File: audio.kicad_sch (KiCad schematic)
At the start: 36 parts, among them J16 Conn_01x02, J20 Audio Output, Q5 2N3904, Q6 2N3904, Q7 2N3904, Q8 2N7000

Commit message: Small drawing cleanups.
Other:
- company: (none) -> EZ Electronics
- title: (none) -> Arduino Mega2560 K3NG Keyer - Audio Circuits
- moved on the sheet: C10, C11, C12, C13, C14, C15, C16, C17, C8, C9, J20, JP4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

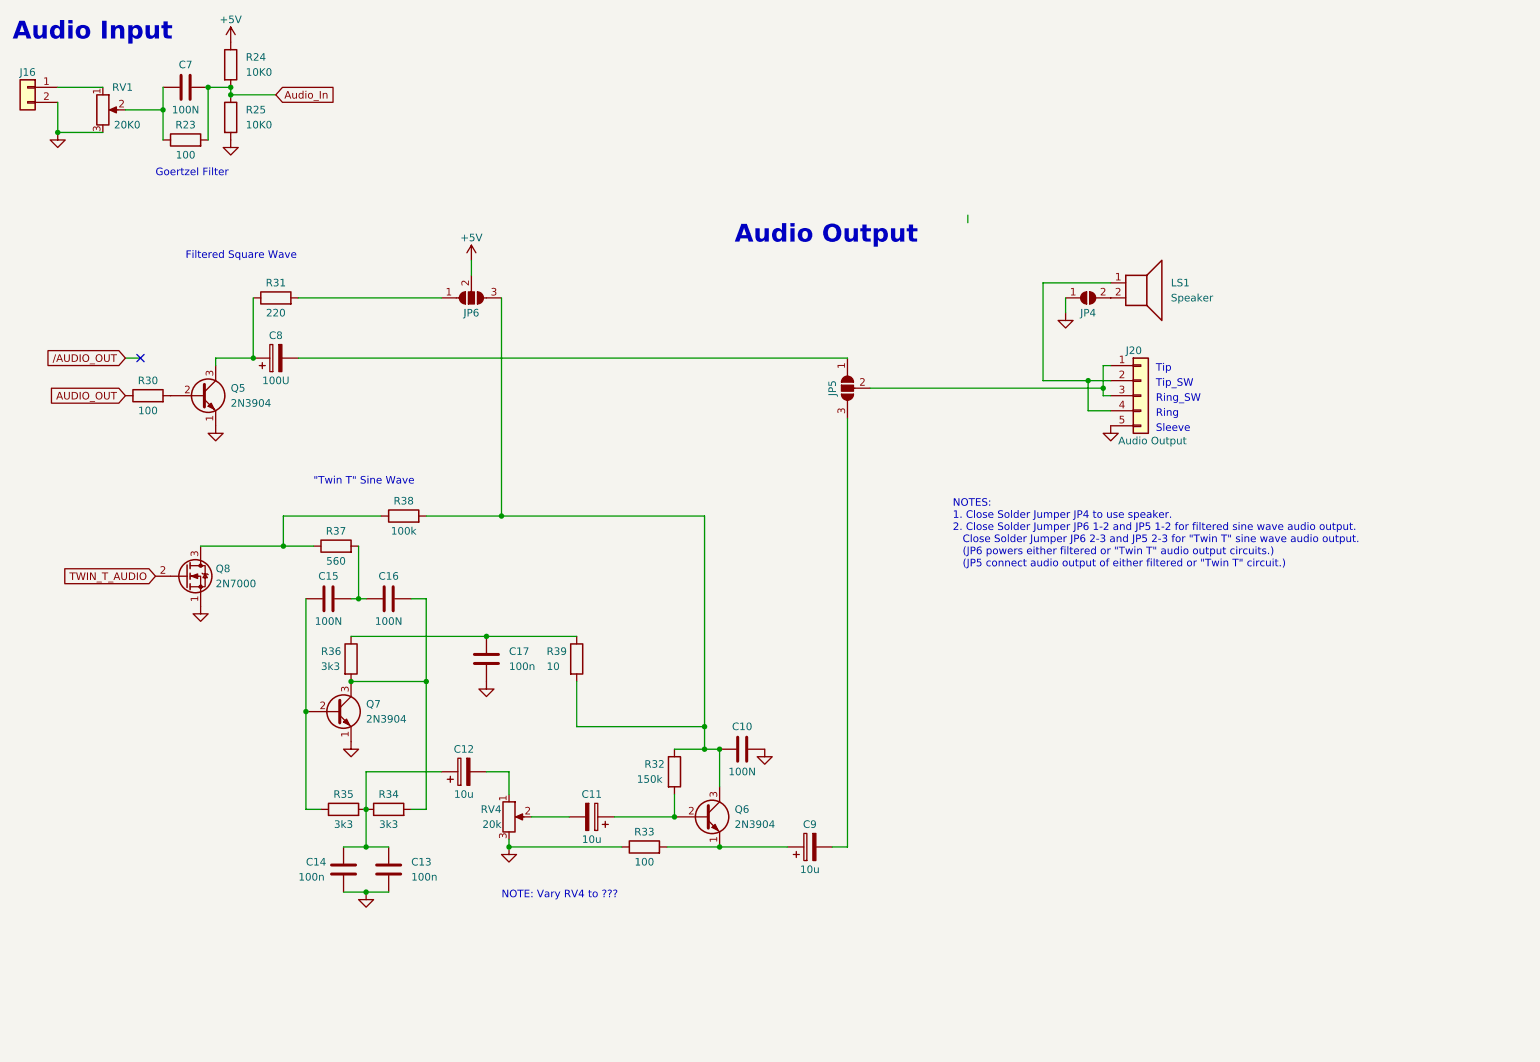
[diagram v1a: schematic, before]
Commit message: Minor changes. Added mounting holes.
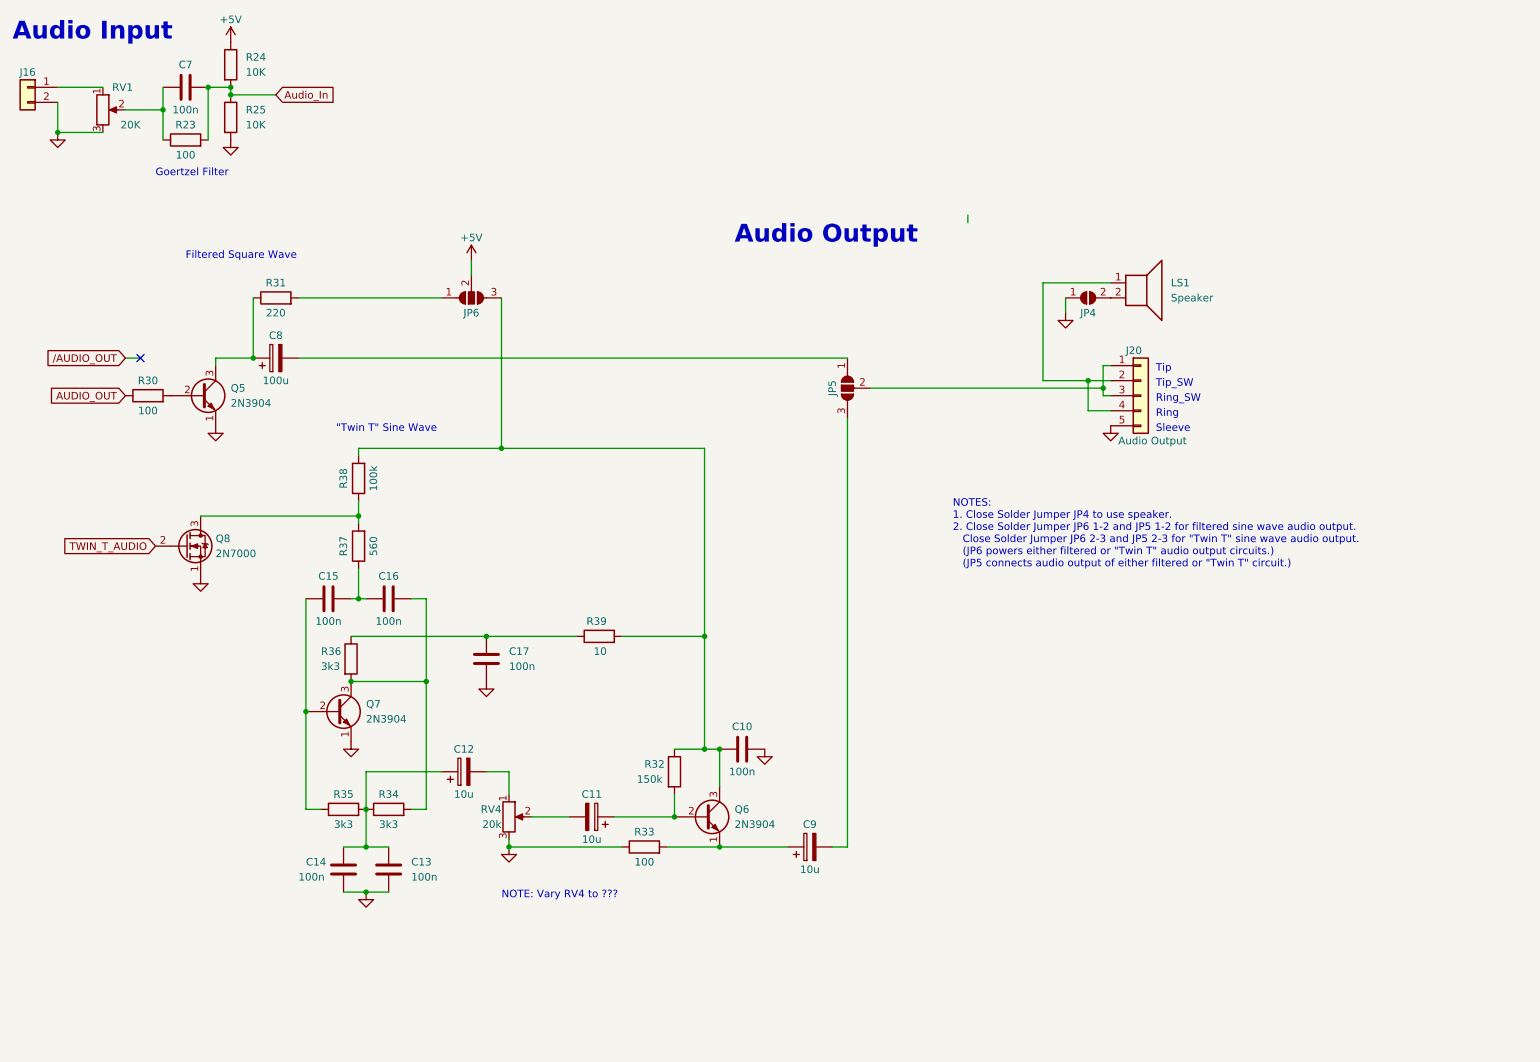
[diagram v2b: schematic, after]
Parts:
- C10, C15, C16, C7: value 100N -> 100n; footprint (none) -> Capacitor_SMD:C_1206_3216Metric; JLCPCB_PN (none) -> C3839854
- C13, C14, C17: footprint (none) -> Capacitor_SMD:C_1206_3216Metric; JLCPCB_PN (none) -> C3839854
- C8: value 100U -> 100u
- R24, R25: value 10K0 -> 10K
- RV1: value 20K0 -> 20K
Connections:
- net at C15.2, C16.1: now also R37.1; no longer R37.2
- net at Q8.3 (D), R38.1: now also R37.2; no longer R37.1
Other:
- note added: "NOTES: 1. Close Solder Jumper JP4 to use speaker. 2. Close Solder Jumper JP6 1-2 and JP5 1-2 for filtered sine wave audio output. Close Solder Jumper JP6 2-3 and JP5 2-3 for "Twin T" sine wave audio output. (JP6 powers either filtered or "Twin T" audio output circuits.) (JP5 connects audio output of either filtered or "Twin T" circuit.)"
- note removed: "NOTES: 1. Close Solder Jumper JP4 to use speaker. 2. Close Solder Jumper JP6 1-2 and JP5 1-2 for filtered sine wave audio output. Close Solder Jumper JP6 2-3 and JP5 2-3 for "Twin T" sine wave audio output. (JP6 powers either filtered or "Twin T" audio output circuits.) (JP5 connect audio output of either filtered or "Twin T" circuit.)"
- moved on the sheet: Q8, R37, R38, R39

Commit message: Added multi-hole strips to unused pins on Arduino Mega 2560 microprocessor. Also, some minor changes.
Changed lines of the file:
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@@
-    (stroke (width 0) (type default))
-  )
-  (wire (pts (xy 180.34 53.34) (xy 180.34 54.61))
     (stroke (width 0) (type default))
   )

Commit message: First attempt at assigning footprints and JLCPCB part numbers.
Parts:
- removed LS1: Speaker, symbol Device:Speaker
- added J55: Conn_01x02, Connector_PinHeader_2.54mm:PinHeader_1x02_P2.54mm_Vertical, symbol Connector_Generic:Conn_01x02
- C11, C12, C9: footprint (none) -> Capacitor_SMD:C_Elec_4x5.4; JLCPCB_PN (none) -> C970654
- C8: footprint (none) -> Capacitor_SMD:C_Elec_6.3x5.8; JLCPCB_PN (none) -> C2972715
- J16: footprint (none) -> Connector_PinHeader_2.54mm:PinHeader_1x02_P2.54mm_Vertical; JLCPCB_PN (none) -> DNP
- J20: footprint (none) -> Connector_PinHeader_2.54mm:PinHeader_1x05_P2.54mm_Vertical; JLCPCB_PN (none) -> DNP
- JP4: footprint (none) -> Jumper:SolderJumper-2_P1.3mm_Open_TrianglePad1.0x1.5mm; JLCPCB_PN (none) -> DNP
- JP5, JP6: footprint (none) -> Jumper:SolderJumper-3_P2.0mm_Open_TrianglePad1.0x1.5mm_NumberLabels; JLCPCB_PN (none) -> DNP
- Q5, Q6, Q7: footprint Package_TO_SOT_THT:TO-92_Inline -> Package_TO_SOT_SMD:SOT-23; JLCPCB_PN (none) -> C18536
- Q8: footprint Package_TO_SOT_THT:TO-92_Inline -> Package_TO_SOT_SMD:SOT-23; JLCPCB_PN (none) -> C414015
- R23, R30, R33: value 100 -> 100R; footprint (none) -> Resistor_SMD:R_0805_2012Metric; JLCPCB_PN (none) -> C17408
- R24, R25: value 10K -> 10k; footprint (none) -> Resistor_SMD:R_0805_2012Metric; JLCPCB_PN (none) -> C17414
- R31: value 220 -> 220R; footprint (none) -> Resistor_SMD:R_0805_2012Metric; JLCPCB_PN (none) -> C441976
- R32: footprint (none) -> Resistor_SMD:R_0805_2012Metric; JLCPCB_PN (none) -> C543493
- R34, R35, R36: footprint (none) -> Resistor_SMD:R_0805_2012Metric; JLCPCB_PN (none) -> C702834
- R37: value 560 -> 560R; footprint (none) -> Resistor_SMD:R_0805_2012Metric; JLCPCB_PN (none) -> C441979
- R38: footprint (none) -> Resistor_SMD:R_0805_2012Metric; JLCPCB_PN (none) -> C441992
- R39: value 10 -> 10R; footprint (none) -> Resistor_SMD:R_0805_2012Metric; JLCPCB_PN (none) -> C17415
- RV1: value 20K -> 20k; footprint (none) -> Resistor_SMD:R_0805_2012Metric; JLCPCB_PN (none) -> C4340265
- RV4: footprint (none) -> Resistor_SMD:R_0805_2012Metric; JLCPCB_PN (none) -> C4340265
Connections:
- net at J20.2 (Pin_2), J20.4 (Pin_4): now also J55.1 (Pin_1)

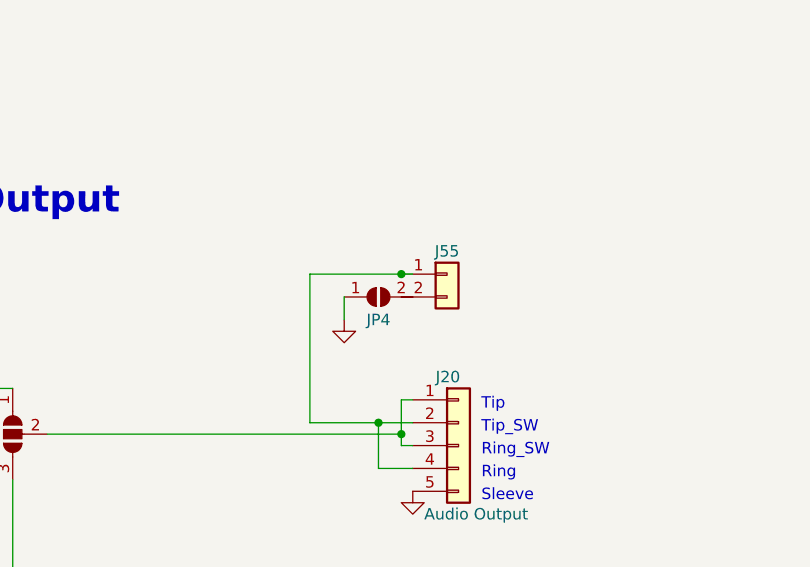
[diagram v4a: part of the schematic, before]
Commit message: Added PWR_FLAG and others to correct ERC errors. All ERC errors corrected; no errors or warnings present.
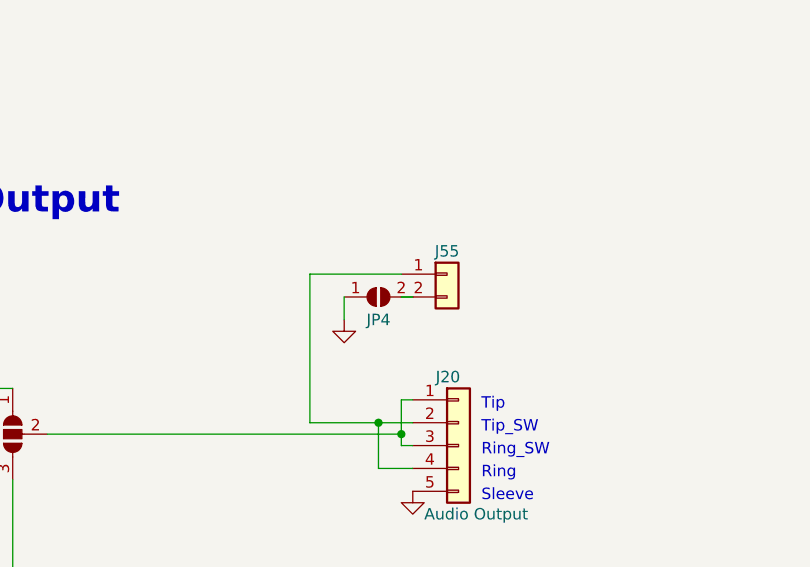
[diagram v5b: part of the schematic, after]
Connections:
- net at JP4.2 (B): now also J55.2 (Pin_2)
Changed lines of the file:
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@@
   (junction (at 200.66 81.28) (diameter 0) (color 0 0 0 0)
-  )
-  (junction (at 203.2 64.77) (diameter 0) (color 0 0 0 0)
   )
   (junction (at 101.6 92.71) (diameter 0) (color 0 0 0 0)
@@
     (stroke (width 0) (type default))
   )
-  (wire (pts (xy 203.2 64.77) (xy 204.47 64.77))
-    (stroke (width 0) (type default))
-  )
   (wire (pts (xy 52.07 31.75) (xy 55.88 31.75))
     (stroke (width 0) (type default))
@@
     (stroke (width 0) (type default))
   )
+  (wire (pts (xy 204.47 67.31) (xy 203.2 67.31))
+    (stroke (width 0) (type default))
+  )

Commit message: Changed many capacitor part numbers.
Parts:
- C10, C13, C14, C15, C16, C17, C7: footprint Capacitor_SMD:C_1206_3216Metric -> Capacitor_SMD:C_0603_1608Metric; JLCPCB_PN C3839854 -> C14663
- C11, C12, C9: footprint Capacitor_SMD:C_Elec_4x5.4 -> Capacitor_Tantalum_SMD:CP_EIA-1608-08_AVX-J; JLCPCB_PN C970654 -> C1952781
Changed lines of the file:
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@@
       (effects (font (size 1.27 1.27)))
     )
-    (property "Footprint" "Capacitor_SMD:C_1206_3216Metric" (at 86.36 117.1448 0)
+    (property "Footprint" "Capacitor_SMD:C_0603_1608Metric" (at 86.36 117.1448 0)
       (effects (font (size 1.27 1.27)) hide)
     )
@@
       (effects (font (size 1.27 1.27)) hide)
     )
-    (property "JLCPCB_PN" "C3839854" (at 82.55 118.11 0)
+    (property "JLCPCB_PN" "C14663" (at 82.55 118.11 0)
       (effects (font (size 1.27 1.27)) hide)
     )
@@
       (effects (font (size 1.27 1.27)))
     )
-    (property "Footprint" "Capacitor_SMD:C_1206_3216Metric" (at 76.2 117.1448 0)
+    (property "Footprint" "Capacitor_SMD:C_0603_1608Metric" (at 76.2 117.1448 0)
       (effects (font (size 1.27 1.27)) hide)
     )
@@
       (effects (font (size 1.27 1.27)) hide)
     )
-    (property "JLCPCB_PN" "C3839854" (at 72.39 118.11 0)
+    (property "JLCPCB_PN" "C14663" (at 72.39 118.11 0)
       (effects (font (size 1.27 1.27)) hide)
     )
@@
       (effects (font (size 1.27 1.27)))
     )
-    (property "Footprint" "Capacitor_SMD:C_Elec_4x5.4" (at 157.48 159.0548 0)
+    (property "Footprint" "Capacitor_Tantalum_SMD:CP_EIA-1608-08_AVX-J" (at 157.48 159.0548 0)
       (effects (font (size 1.27 1.27)) hide)
     )
@@
       (effects (font (size 1.27 1.27)) hide)
     )
-    (property "JLCPCB_PN" "C970654" (at 153.67 160.02 0)
+    (property "JLCPCB_PN" "C1952781" (at 153.67 160.02 0)
       (effects (font (size 1.27 1.27)) hide)
     )
@@
       (effects (font (size 1.27 1.27)))
     )
-    (property "Footprint" "Capacitor_SMD:C_1206_3216Metric" (at 52.07 30.7848 0)
+    (property "Footprint" "Capacitor_SMD:C_0603_1608Metric" (at 52.07 30.7848 0)
       (effects (font (size 1.27 1.27)) hide)
     )
@@
       (effects (font (size 1.27 1.27)) hide)
     )
-    (property "JLCPCB_PN" "C3839854" (at 48.26 31.75 0)
+    (property "JLCPCB_PN" "C14663" (at 48.26 31.75 0)
       (effects (font (size 1.27 1.27)) hide)
     )
@@
       (effects (font (size 1.27 1.27)))
     )
-    (property "Footprint" "Capacitor_SMD:C_1206_3216Metric" (at 146.05 142.5448 0)
+    (property "Footprint" "Capacitor_SMD:C_0603_1608Metric" (at 146.05 142.5448 0)
       (effects (font (size 1.27 1.27)) hide)
     )
@@
       (effects (font (size 1.27 1.27)) hide)
     )
-    (property "JLCPCB_PN" "C3839854" (at 142.24 143.51 0)
+    (property "JLCPCB_PN" "C14663" (at 142.24 143.51 0)
       (effects (font (size 1.27 1.27)) hide)
     )
@@
       (effects (font (size 1.27 1.27)))
     )
-    (property "Footprint" "Capacitor_SMD:C_Elec_4x5.4" (at 99.06 146.3548 0)
+    (property "Footprint" "Capacitor_Tantalum_SMD:CP_EIA-1608-08_AVX-J" (at 99.06 146.3548 0)
       (effects (font (size 1.27 1.27)) hide)
     )
@@
       (effects (font (size 1.27 1.27)) hide)
     )
-    (property "JLCPCB_PN" "C970654" (at 95.25 147.32 0)
+    (property "JLCPCB_PN" "C1952781" (at 95.25 147.32 0)
       (effects (font (size 1.27 1.27)) hide)
     )
@@
       (effects (font (size 1.27 1.27)))
     )
-    (property "Footprint" "Capacitor_SMD:C_Elec_4x5.4" (at 113.03 153.9748 0)
+    (property "Footprint" "Capacitor_Tantalum_SMD:CP_EIA-1608-08_AVX-J" (at 113.03 153.9748 0)
       (effects (font (size 1.27 1.27)) hide)
     )
@@
       (effects (font (size 1.27 1.27)) hide)
     )
-    (property "JLCPCB_PN" "C970654" (at 116.84 154.94 0)
+    (property "JLCPCB_PN" "C1952781" (at 116.84 154.94 0)
       (effects (font (size 1.27 1.27)) hide)
     )
@@
       (effects (font (size 1.27 1.27)) (justify left))
     )
-    (property "Footprint" "Capacitor_SMD:C_1206_3216Metric" (at 83.5152 167.64 0)
+    (property "Footprint" "Capacitor_SMD:C_0603_1608Metric" (at 83.5152 167.64 0)
       (effects (font (size 1.27 1.27)) hide)
     )
@@
       (effects (font (size 1.27 1.27)) hide)
     )
-    (property "JLCPCB_PN" "C3839854" (at 82.55 163.83 0)
+    (property "JLCPCB_PN" "C14663" (at 82.55 163.83 0)
       (effects (font (size 1.27 1.27)) hide)
     )
@@
       (effects (font (size 1.27 1.27)) (justify left))
     )
-    (property "Footprint" "Capacitor_SMD:C_1206_3216Metric" (at 100.0252 132.08 0)
+    (property "Footprint" "Capacitor_SMD:C_0603_1608Metric" (at 100.0252 132.08 0)
       (effects (font (size 1.27 1.27)) hide)
     )
@@
       (effects (font (size 1.27 1.27)) hide)
     )
-    (property "JLCPCB_PN" "C3839854" (at 99.06 128.27 0)
+    (property "JLCPCB_PN" "C14663" (at 99.06 128.27 0)
       (effects (font (size 1.27 1.27)) hide)
     )
@@
       (effects (font (size 1.27 1.27)) (justify left))
     )
-    (property "Footprint" "Capacitor_SMD:C_1206_3216Metric" (at 75.8952 167.64 0)
+    (property "Footprint" "Capacitor_SMD:C_0603_1608Metric" (at 75.8952 167.64 0)
       (effects (font (size 1.27 1.27)) hide)
     )
@@
       (effects (font (size 1.27 1.27)) hide)
     )
-    (property "JLCPCB_PN" "C3839854" (at 74.93 163.83 0)
-      (effects (font (size 1.27 1.27)) hide)
-    )
+    (property "JLCPCB_PN" "C14663" (at 74.93 163.83 0)
+      (effects (font (size 1.27 1.27)) hide)
+    )

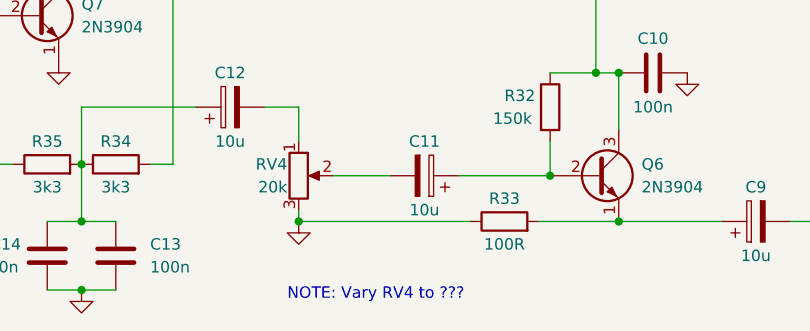
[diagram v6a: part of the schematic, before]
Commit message: Fixed variable resistor parts.
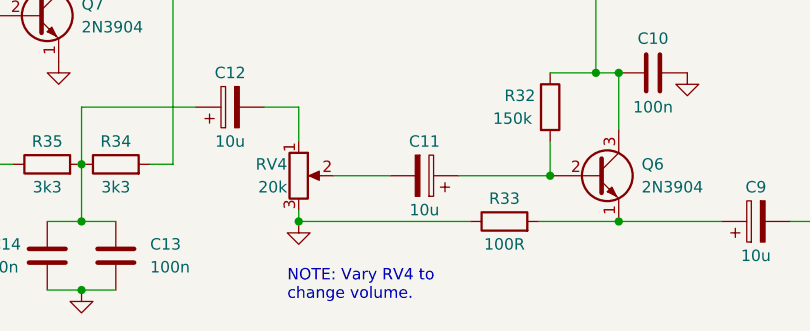
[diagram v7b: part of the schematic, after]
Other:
- note added: "NOTE: Vary RV4 to change volume."
- note removed: "NOTE: Vary RV4 to ???"
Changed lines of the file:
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@@
     (effects (font (size 1.27 1.27)) (justify left bottom))
   )
-  (text "NOTE: Vary RV4 to ???" (at 101.6 168.91 0)
+  (text "NOTE: Vary RV4 to\nchange volume." (at 101.6 168.91 0)
     (effects (font (size 1.27 1.27)) (justify left bottom))
   )

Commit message: Fixed variable resistor parts (forgot to save before committing).
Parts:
- RV1, RV4: footprint Resistor_SMD:R_0805_2012Metric -> Potentiometer_SMD:Potentiometer_Bourns_3314J_Vertical; JLCPCB_PN C4340265 -> C124621
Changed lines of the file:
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@@
       (effects (font (size 1.27 1.27)) (justify right))
     )
-    (property "Footprint" "Resistor_SMD:R_0805_2012Metric" (at 102.87 154.94 0)
+    (property "Footprint" "Potentiometer_SMD:Potentiometer_Bourns_3314J_Vertical" (at 102.87 154.94 0)
       (effects (font (size 1.27 1.27)) hide)
     )
@@
       (effects (font (size 1.27 1.27)) hide)
     )
-    (property "JLCPCB_PN" "C4340265" (at 102.87 154.94 0)
+    (property "JLCPCB_PN" "C124621" (at 102.87 154.94 0)
       (effects (font (size 1.27 1.27)) hide)
     )
@@
       (effects (font (size 1.27 1.27)) (justify right))
     )
-    (property "Footprint" "Resistor_SMD:R_0805_2012Metric" (at 34.29 35.56 0)
+    (property "Footprint" "Potentiometer_SMD:Potentiometer_Bourns_3314J_Vertical" (at 34.29 35.56 0)
       (effects (font (size 1.27 1.27)) hide)
     )
@@
       (effects (font (size 1.27 1.27)) hide)
     )
-    (property "JLCPCB_PN" "C4340265" (at 34.29 35.56 0)
-      (effects (font (size 1.27 1.27)) hide)
-    )
+    (property "JLCPCB_PN" "C124621" (at 34.29 35.56 0)
+      (effects (font (size 1.27 1.27)) hide)
+    )
